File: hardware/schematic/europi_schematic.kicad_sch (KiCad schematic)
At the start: 110 parts, among them J1 Output 1 Jack, J2 Output 2 Jack, J3 Output 3 Jack, J4 Output 4 Jack, J5 Output 5 Jack, J6 Output 6 Jack, J7 Digital Input Jack, J8 Analogue Input Jack, Q1 2N2222, SW1 SW_Push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

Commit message: Fix MCP6002 Power Rail Labeling
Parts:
- removed C1: 1uF, symbol Device:C_Polarized
- removed Reference?: +3.3V, symbol text:TEXT
- C10, C11, C12, C13, C14, C3, C4, C5, C6, C9: symbol Device:C -> Device:CP
- C2: symbol Device:C_Polarized -> Device:C
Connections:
- net GND: now also O?.4 (V-); no longer O?.8 (V+)
- net at Reference?.1: now also O?.8 (V+); no longer O?.4 (V-)

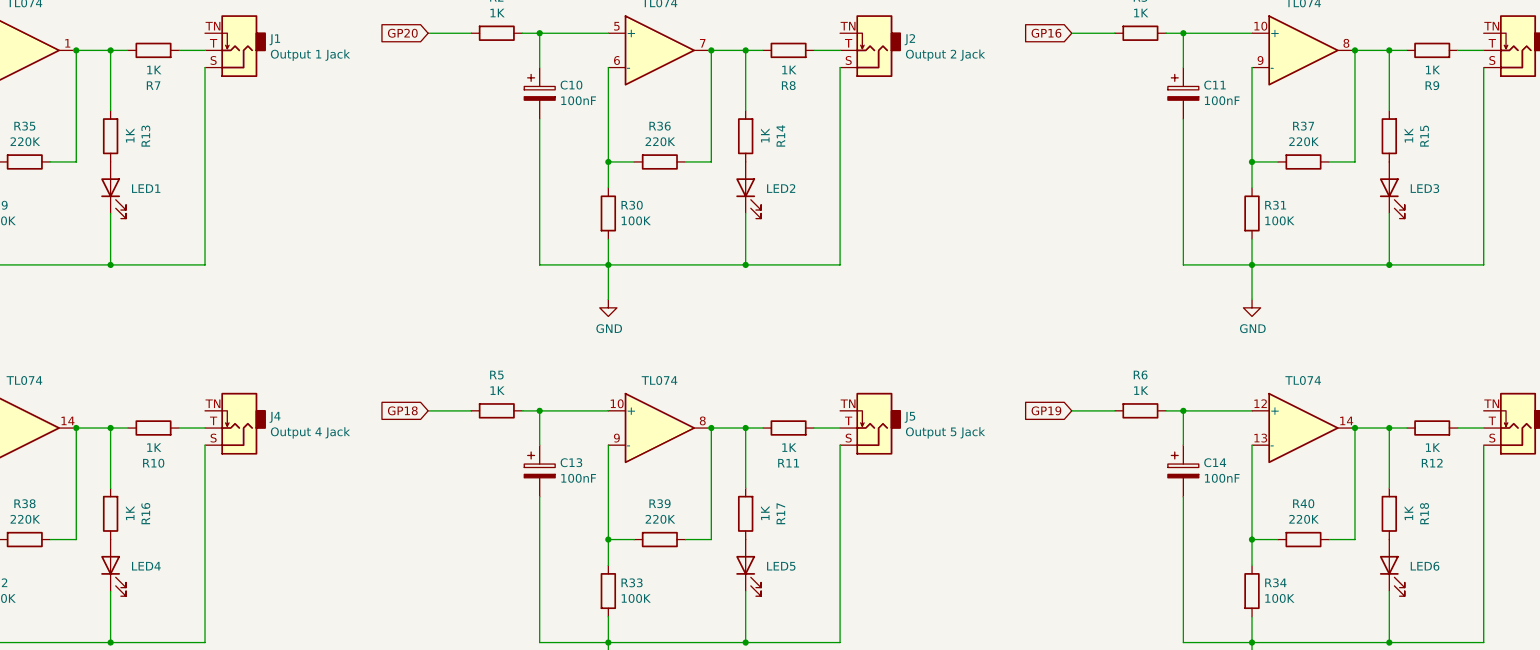
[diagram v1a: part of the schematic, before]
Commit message: Change LED resistors to 4k7
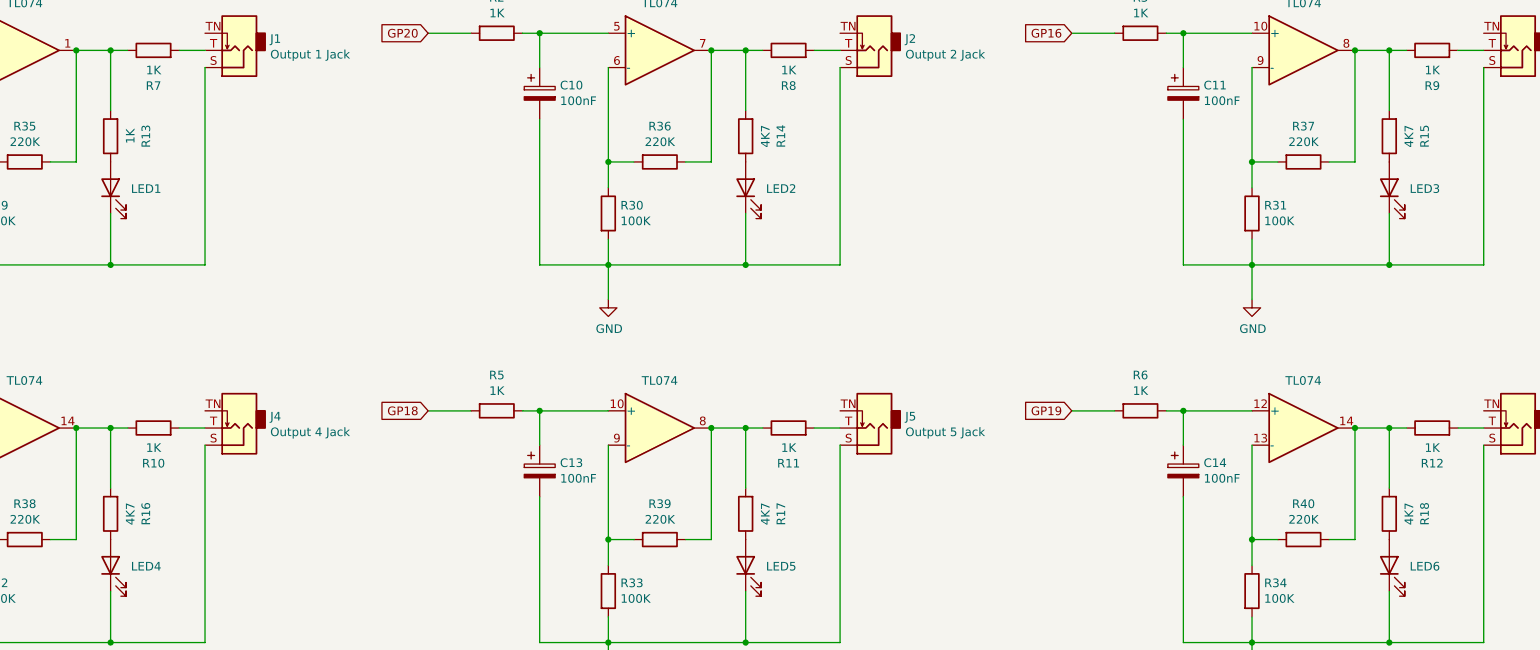
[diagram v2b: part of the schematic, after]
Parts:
- R14, R15, R16, R17, R18: value 1K -> 4K7
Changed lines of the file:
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@@
     (in_bom yes) (on_board yes)
     (property "Reference" "R14" (id 0) (at 266.8778 50.8 90))
-    (property "Value" "1K" (id 1) (at 264.5664 50.8 90))
+    (property "Value" "4K7" (id 1) (at 264.5664 50.8 90))
     (property "Footprint" "" (id 2) (at 263.398 50.8 90)
       (effects (font (size 1.27 1.27)) hide)
@@
     (in_bom yes) (on_board yes)
     (property "Reference" "R15" (id 0) (at 362.1278 50.8 90))
-    (property "Value" "1K" (id 1) (at 359.8164 50.8 90))
+    (property "Value" "4K7" (id 1) (at 359.8164 50.8 90))
     (property "Footprint" "" (id 2) (at 358.648 50.8 90)
       (effects (font (size 1.27 1.27)) hide)
@@
     (in_bom yes) (on_board yes)
     (property "Reference" "R16" (id 0) (at 172.8978 106.68 90))
-    (property "Value" "1K" (id 1) (at 170.5864 106.68 90))
+    (property "Value" "4K7" (id 1) (at 170.5864 106.68 90))
     (property "Footprint" "" (id 2) (at 169.418 106.68 90)
       (effects (font (size 1.27 1.27)) hide)
@@
     (in_bom yes) (on_board yes)
     (property "Reference" "R17" (id 0) (at 266.8778 106.68 90))
-    (property "Value" "1K" (id 1) (at 264.5664 106.68 90))
+    (property "Value" "4K7" (id 1) (at 264.5664 106.68 90))
     (property "Footprint" "" (id 2) (at 263.398 106.68 90)
       (effects (font (size 1.27 1.27)) hide)
@@
     (in_bom yes) (on_board yes)
     (property "Reference" "R18" (id 0) (at 362.1278 106.68 90))
-    (property "Value" "1K" (id 1) (at 359.8164 106.68 90))
+    (property "Value" "4K7" (id 1) (at 359.8164 106.68 90))
     (property "Footprint" "" (id 2) (at 358.648 106.68 90)
       (effects (font (size 1.27 1.27)) hide)
@@
     )
     (path "/00000000-0000-0000-0000-0000619dfa13"
-      (reference "R14") (unit 1) (value "1K") (footprint "")
+      (reference "R14") (unit 1) (value "4K7") (footprint "")
     )
     (path "/00000000-0000-0000-0000-0000619e5733"
-      (reference "R15") (unit 1) (value "1K") (footprint "")
+      (reference "R15") (unit 1) (value "4K7") (footprint "")
     )
     (path "/00000000-0000-0000-0000-0000619e9956"
-      (reference "R16") (unit 1) (value "1K") (footprint "")
+      (reference "R16") (unit 1) (value "4K7") (footprint "")
     )
     (path "/00000000-0000-0000-0000-0000619ee4a3"
-      (reference "R17") (unit 1) (value "1K") (footprint "")
+      (reference "R17") (unit 1) (value "4K7") (footprint "")
     )
     (path "/00000000-0000-0000-0000-0000619f2fc4"
-      (reference "R18") (unit 1) (value "1K") (footprint "")
+      (reference "R18") (unit 1) (value "4K7") (footprint "")
     )
     (path "/00000000-0000-0000-0000-000062157405"
